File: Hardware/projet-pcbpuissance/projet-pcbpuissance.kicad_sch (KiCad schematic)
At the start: 35 parts, among them J2 Conn_01x02, J3 Conn_01x02, J4 Conn_01x02, U1 MAX5033DUSA+, U2 MAX5033DUSA+

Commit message: Modif PCB
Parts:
- D2, D6: footprint Diode_SMD:D_SMA_Handsoldering -> Diode_SMD:D_2114_3652Metric_Pad1.85x3.75mm_HandSolder
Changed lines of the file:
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@@
       (effects (font (size 1.27 1.27)) (justify left))
     )
-    (property "Footprint" "Diode_SMD:D_SMA_Handsoldering" (at 181.61 74.93 0)
+    (property "Footprint" "Diode_SMD:D_2114_3652Metric_Pad1.85x3.75mm_HandSolder" (at 181.61 74.93 0)
       (effects (font (size 1.27 1.27)) hide)
     )
@@
       (effects (font (size 1.27 1.27)) (justify left))
     )
-    (property "Footprint" "Diode_SMD:D_SMA_Handsoldering" (at 87.63 74.93 0)
-      (effects (font (size 1.27 1.27)) hide)
-    )
+    (property "Footprint" "Diode_SMD:D_2114_3652Metric_Pad1.85x3.75mm_HandSolder" (at 87.63 74.93 0)
+      (effects (font (size 1.27 1.27)) hide)
+    )

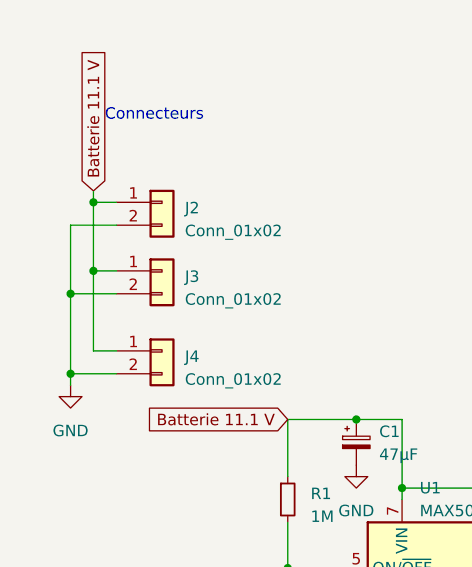
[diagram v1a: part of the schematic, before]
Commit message: update with bigger vias and fix unrouted tracks
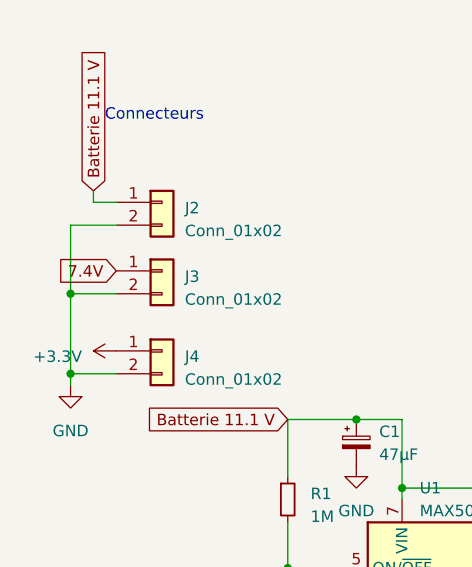
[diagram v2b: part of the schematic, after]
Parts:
- J2, J3, J4: footprint Connector_JST:JST_XH_B2B-XH-AM_1x02_P2.50mm_Vertical -> Connector_JST:JST_XH_B2B-XH-A_1x02_P2.50mm_Vertical
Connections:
- net +3.3V: now also J4.1 (Pin_1)
- net 7.4V: now also J3.1 (Pin_1)
- net Batterie 11.1 V: no longer J3.1 (Pin_1), J4.1 (Pin_1)
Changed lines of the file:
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@@
   (junction (at 19.05 40.64) (diameter 0) (color 0 0 0 0)
   )
-  (junction (at 21.59 30.48) (diameter 0) (color 0 0 0 0)
-  )
   (junction (at 92.71 71.12) (diameter 0) (color 0 0 0 0)
   )
@@
   (junction (at 63.5 97.79) (diameter 0) (color 0 0 0 0)
   )
-  (junction (at 21.59 38.1) (diameter 0) (color 0 0 0 0)
-  )
   (junction (at 55.88 62.23) (diameter 0) (color 0 0 0 0)
   )
@@
     (stroke (width 0) (type default))
   )
-  (wire (pts (xy 21.59 46.99) (xy 21.59 38.1))
-    (stroke (width 0) (type default))
-  )
   (wire (pts (xy 43.18 66.04) (xy 43.18 71.12))
     (stroke (width 0) (type default))
@@
     (stroke (width 0) (type default))
   )
-  (wire (pts (xy 21.59 38.1) (xy 21.59 30.48))
-    (stroke (width 0) (type default))
-  )
   (wire (pts (xy 186.69 87.63) (xy 186.69 82.55))
     (stroke (width 0) (type default))
@@
     (stroke (width 0) (type default))
   )
-  (wire (pts (xy 24.13 46.99) (xy 21.59 46.99))
-    (stroke (width 0) (type default))
-  )
   (wire (pts (xy 76.2 71.12) (xy 87.63 71.12))
     (stroke (width 0) (type default))
@@
   )
   (wire (pts (xy 57.15 101.6) (xy 63.5 101.6))
-    (stroke (width 0) (type default))
-  )
-  (wire (pts (xy 24.13 38.1) (xy 21.59 38.1))
     (stroke (width 0) (type default))
   )
@@
     )
   )
+  (global_label "7.4V" (shape input) (at 24.13 38.1 180) (fields_autoplaced)
+    (effects (font (size 1.27 1.27)) (justify right))
+    (property "Intersheetrefs" "${INTERSHEET_REFS}" (at 17.1118 38.1 0)
+      (effects (font (size 1.27 1.27)) (justify right) hide)
+    )
+  )
   (global_label "7.4V" (shape input) (at 212.09 71.12 0) (fields_autoplaced)
     (effects (font (size 1.27 1.27)) (justify left))
@@
       (effects (font (size 1.27 1.27)) (justify left))
     )
-    (property "Footprint" "Connector_JST:JST_XH_B2B-XH-AM_1x02_P2.50mm_Vertical" (at 29.21 38.1 0)
+    (property "Footprint" "Connector_JST:JST_XH_B2B-XH-A_1x02_P2.50mm_Vertical" (at 29.21 38.1 0)
       (effects (font (size 1.27 1.27)) hide)
     )
@@
       (effects (font (size 1.27 1.27)) (justify left))
     )
-    (property "Footprint" "Connector_JST:JST_XH_B2B-XH-AM_1x02_P2.50mm_Vertical" (at 29.21 46.99 0)
+    (property "Footprint" "Connector_JST:JST_XH_B2B-XH-A_1x02_P2.50mm_Vertical" (at 29.21 46.99 0)
       (effects (font (size 1.27 1.27)) hide)
     )
@@
         (path "/2869d089-2104-43b1-9a93-26592258e38f"
           (reference "R8") (unit 1)
+        )
+      )
+    )
+  )
+  (symbol (lib_id "power:+3.3V") (at 24.13 46.99 90) (unit 1)
+    (in_bom yes) (on_board yes) (dnp no) (fields_autoplaced)
+    (property "Reference" "#PWR015" (at 27.94 46.99 0)
+      (effects (font (size 1.27 1.27)) hide)
+    )
+    (property "Value" "+3.3V" (at 20.32 47.625 90)
+      (effects (font (size 1.27 1.27)) (justify left))
+    )
+    (property "Footprint" "" (at 24.13 46.99 0)
+      (effects (font (size 1.27 1.27)) hide)
+    )
+    (property "Datasheet" "" (at 24.13 46.99 0)
+      (effects (font (size 1.27 1.27)) hide)
+    )
+    (pin "1")
+    (instances
+      (project "projet-pcbpuissance"
+        (path "/2869d089-2104-43b1-9a93-26592258e38f"
+          (reference "#PWR015") (unit 1)
         )
       )
@@
       (effects (font (size 1.27 1.27)) (justify left))
     )
-    (property "Footprint" "Connector_JST:JST_XH_B2B-XH-AM_1x02_P2.50mm_Vertical" (at 29.21 30.48 0)
-      (effects (font (size 1.27 1.27)) hide)
-    )
+    (property "Footprint" "Connector_JST:JST_XH_B2B-XH-A_1x02_P2.50mm_Vertical" (at 29.21 30.48 0)
+      (effects (font (size 1.27 1.27)) hide)
+    )
